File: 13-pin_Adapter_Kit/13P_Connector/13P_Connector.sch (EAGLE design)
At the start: 4 parts

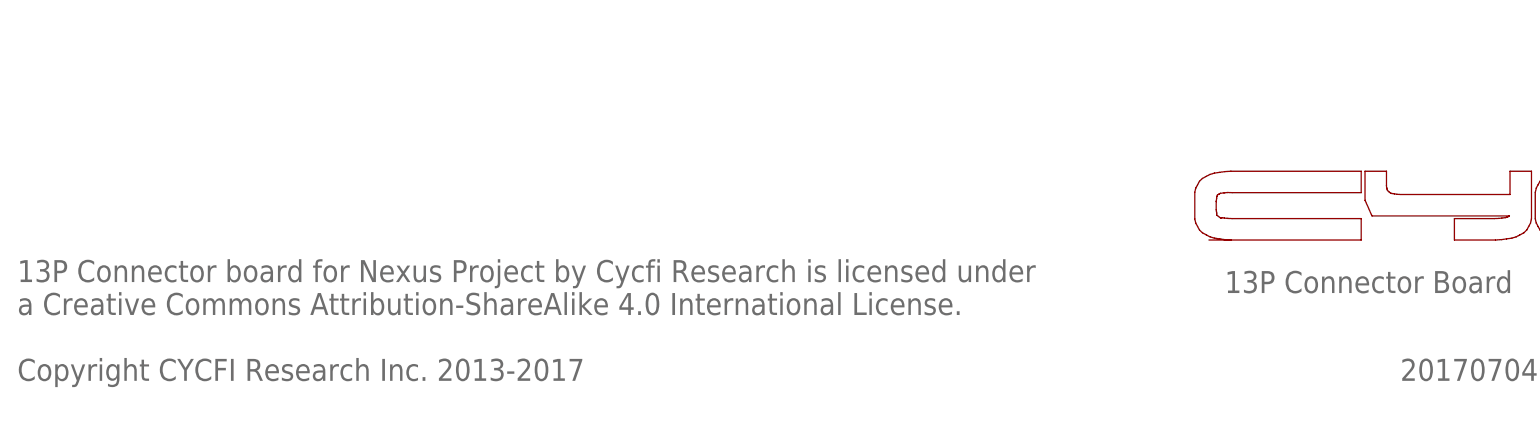
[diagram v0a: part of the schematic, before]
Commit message: Updated Notes "For Nu Project" instead of "Nexus"
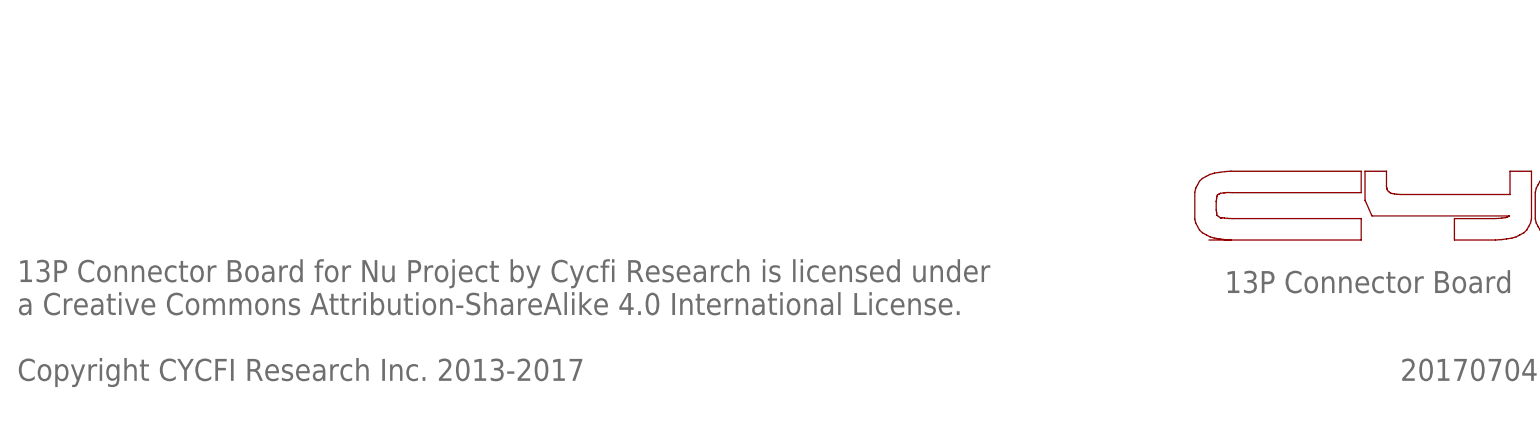
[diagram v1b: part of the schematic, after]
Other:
- note added: "13P Connector Board for Nu Project by Cycfi Research is licensed under a Creative Commons Attribution-ShareAlike 4.0 International License. Copyright CYCFI Research Inc. 2013-2017"
- note removed: "13P Connector board for Nexus Project by Cycfi Research is licensed under a Creative Commons Attribution-ShareAlike 4.0 International License. Copyright CYCFI Research Inc. 2013-2017"
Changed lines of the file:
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@@
 <?xml version="1.0" encoding="utf-8"?>
 <!DOCTYPE eagle SYSTEM "eagle.dtd">
-<eagle version="6.3">
+<eagle version="7.6.0">
 <drawing>
 <settings>
@@
 <sheet>
 <plain>
-<text x="22.86" y="8.89" size="2.54" layer="95">13P Connector board for Nexus Project by Cycfi Research is licensed under
+<text x="22.86" y="8.89" size="2.54" layer="95">13P Connector Board for Nu Project by Cycfi Research is licensed under
 a Creative Commons Attribution-ShareAlike 4.0 International License.
 Copyright CYCFI Research Inc. 2013-2017</text>

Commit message: Updated document number.
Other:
- note added: "2017022"
- note removed: "2017070404"
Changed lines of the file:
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@@
 <wire x1="163.27975" y1="25.186403125" x2="160.73975" y2="25.186403125" width="0" layer="94"/>
 <text x="238.76" y="6.35" size="2.54" layer="95">0.93</text>
-<text x="182.88" y="8.89" size="2.54" layer="95">2017070404</text>
+<text x="185.42" y="11.43" size="2.54" layer="95">2017022</text>
 </plain>
 <instances>
